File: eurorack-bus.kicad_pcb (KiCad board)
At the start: 2 copper layers, 5 parts, among them J1 Conn_02x08_Odd_Even, J3 Conn_02x08_Odd_Even, J4 Conn_02x08_Odd_Even, J5 Conn_02x08_Odd_Even, J6 Conn_02x08_Odd_Even

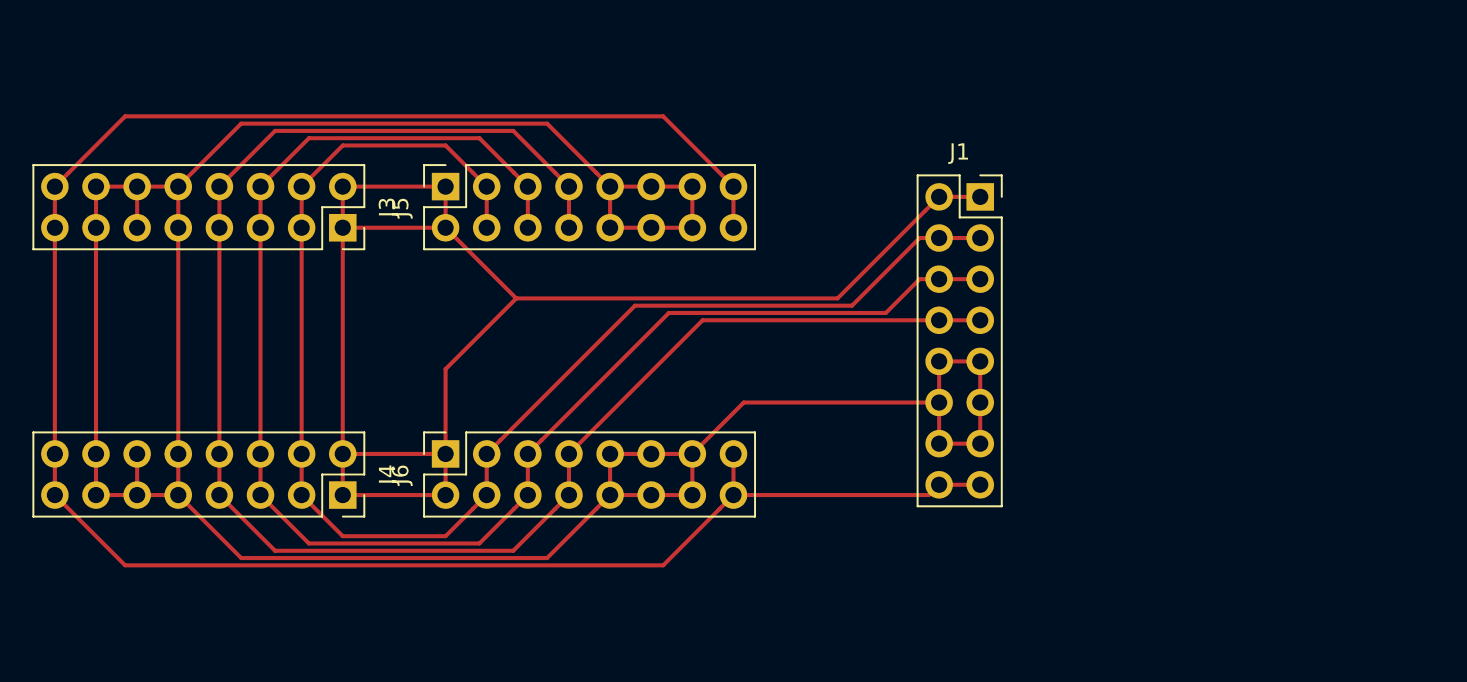
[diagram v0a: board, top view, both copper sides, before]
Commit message: readd conn J2, rm 5v/cv/gt tracks, route
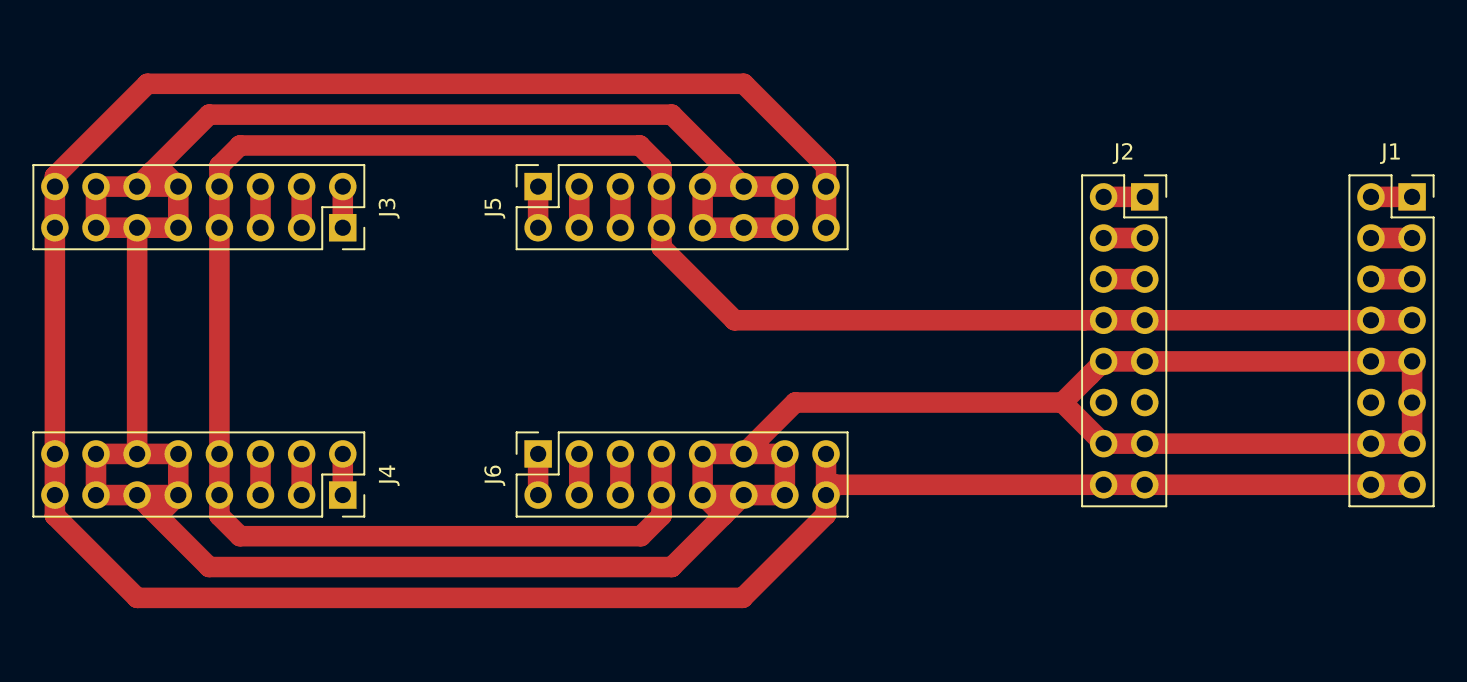
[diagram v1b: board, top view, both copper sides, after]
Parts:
- added J2: Conn_02x08_Odd_Even, Connector_PinSocket_2.54mm:PinSocket_2x08_P2.54mm_Vertical, F.Cu at (151.1, 80.6)
- moved J1 26.7 mm to (167.6, 80.6)
- moved J5 5.72 mm to (113.7, 80.0)
- moved J6 5.72 mm to (113.7, 96.5)
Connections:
- J3 pad 1: Net-(J1-Pad1) -> Net-(J3-Pad1)
- J3 pad 2: Net-(J1-Pad1) -> Net-(J3-Pad1)
- J3 pad 3: Net-(J1-Pad3) -> Net-(J3-Pad3)
- J3 pad 4: Net-(J1-Pad3) -> Net-(J3-Pad3)
- J3 pad 5: Net-(J1-Pad5) -> Net-(J3-Pad5)
- J3 pad 6: Net-(J1-Pad5) -> Net-(J3-Pad5)
- J4 pad 1: Net-(J1-Pad1) -> Net-(J4-Pad1)
- J4 pad 2: Net-(J1-Pad1) -> Net-(J4-Pad1)
- J4 pad 3: Net-(J1-Pad3) -> Net-(J4-Pad3)
- J4 pad 4: Net-(J1-Pad3) -> Net-(J4-Pad3)
- J4 pad 5: Net-(J1-Pad5) -> Net-(J4-Pad5)
- J4 pad 6: Net-(J1-Pad5) -> Net-(J4-Pad5)
- J5 pad 1: Net-(J1-Pad1) -> Net-(J5-Pad1)
- J5 pad 2: Net-(J1-Pad1) -> Net-(J5-Pad1)
- J5 pad 3: Net-(J1-Pad3) -> Net-(J5-Pad3)
- J5 pad 4: Net-(J1-Pad3) -> Net-(J5-Pad3)
- J5 pad 5: Net-(J1-Pad5) -> Net-(J5-Pad5)
- J5 pad 6: Net-(J1-Pad5) -> Net-(J5-Pad5)
- J6 pad 1: Net-(J1-Pad1) -> Net-(J6-Pad1)
- J6 pad 2: Net-(J1-Pad1) -> Net-(J6-Pad1)
- J6 pad 3: Net-(J1-Pad3) -> Net-(J6-Pad3)
- J6 pad 4: Net-(J1-Pad3) -> Net-(J6-Pad3)
- J6 pad 5: Net-(J1-Pad5) -> Net-(J6-Pad5)
- J6 pad 6: Net-(J1-Pad5) -> Net-(J6-Pad5)
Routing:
- net Net-(J1-Pad1): track 98.4 -> 2.54 mm
- net Net-(J1-Pad5): track 94.5 -> 2.54 mm
- net Net-(J1-Pad3): track 87.2 -> 2.54 mm
- net Net-(J1-Pad10): track 175.4 -> 234.7 mm
- net Net-(J1-Pad15): track 130.6 -> 168.9 mm
- net Net-(J1-Pad7): track 101.8 -> 135.3 mm
- net Net-(J6-Pad3): track 0.00 -> 2.59 mm
- net Net-(J6-Pad5): track 0.00 -> 2.54 mm
- net Net-(J6-Pad1): track 0.00 -> 2.54 mm
- net Net-(J4-Pad5): track 0.00 -> 2.54 mm
- net Net-(J4-Pad3): track 0.00 -> 2.54 mm
- net Net-(J4-Pad1): track 0.00 -> 2.54 mm
- net Net-(J5-Pad5): track 0.00 -> 2.54 mm
- net Net-(J5-Pad3): track 0.00 -> 2.54 mm
- net Net-(J5-Pad1): track 0.00 -> 2.54 mm
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- added copper zone on F.Cu, net Net-(J1-Pad10)

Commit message: space things out a little further
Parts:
- moved J5 1.27 mm to (113.7, 78.7)
- moved J6 1.27 mm to (113.7, 97.8)
- moved J3 1.27 mm to (101.6, 81.3)
- moved J4 1.27 mm to (101.6, 100.3)
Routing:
- net Net-(J1-Pad15): track 168.9 -> 172.3 mm
- net Net-(J1-Pad10): track 234.7 -> 237.6 mm
- net Net-(J1-Pad7): track 135.3 -> 137.1 mm

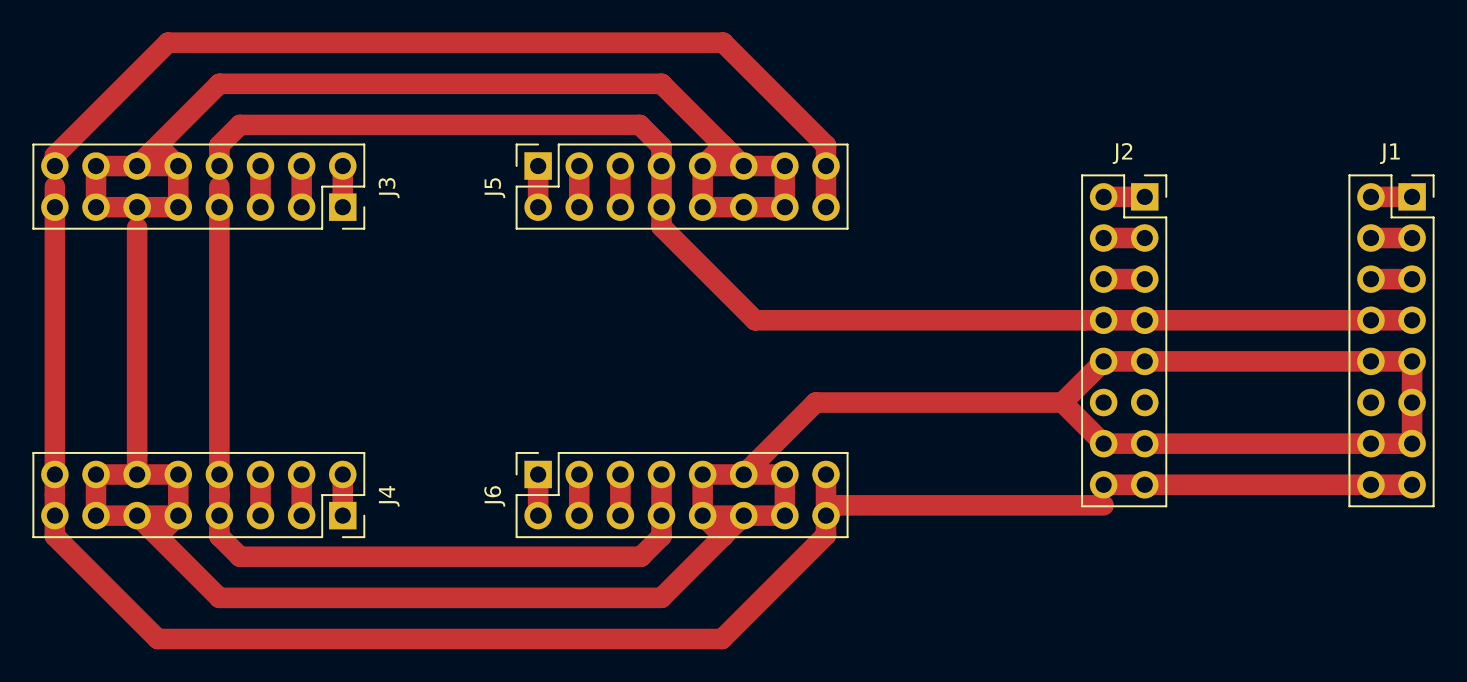
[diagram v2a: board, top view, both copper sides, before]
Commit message: fixup a few traces that should be connected
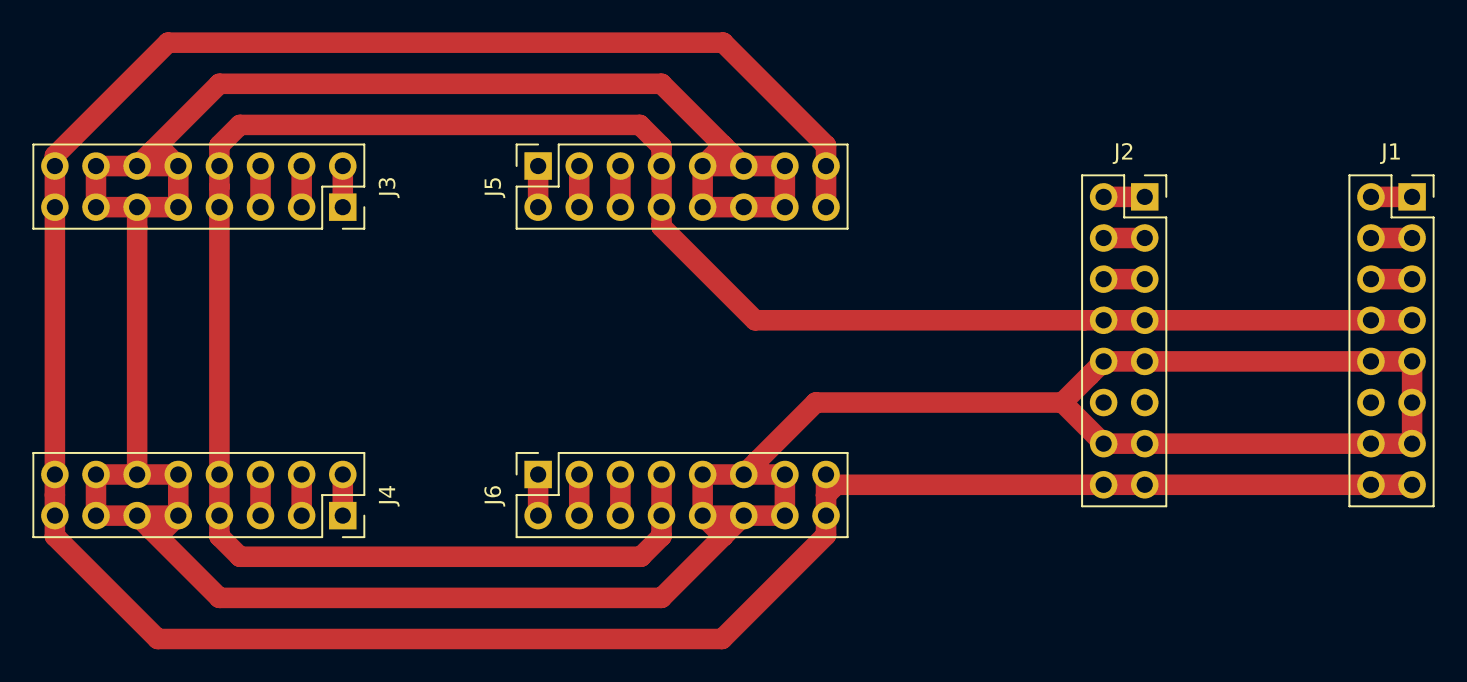
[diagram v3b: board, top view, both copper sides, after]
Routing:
- net Net-(J1-Pad10): track 237.6 -> 238.8 mm
- net Net-(J1-Pad7): track 137.1 -> 138.4 mm
- net Net-(J1-Pad15): track 172.3 -> 173.6 mm
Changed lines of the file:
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@@
     (thickness 1.6)
     (drawings 0)
-    (tracks 103)
+    (tracks 104)
     (zones 0)
     (modules 6)
@@
   (segment (start 93.98 77.47) (end 95.25 76.2) (width 1.27) (layer F.Cu) (net 4))
   (segment (start 95.25 76.2) (end 119.947081 76.2) (width 1.27) (layer F.Cu) (net 4))
-  (segment (start 93.98 99.06) (end 93.98 80.01) (width 1.27) (layer F.Cu) (net 4))
   (segment (start 121.285 78.74) (end 121.285 81.28) (width 1.27) (layer F.Cu) (net 4))
   (segment (start 121.285 97.79) (end 121.285 100.33) (width 1.27) (layer F.Cu) (net 4))
@@
   (segment (start 121.285 101.6) (end 120.015 102.87) (width 1.27) (layer F.Cu) (net 4))
   (segment (start 121.285 100.33) (end 121.285 101.6) (width 1.27) (layer F.Cu) (net 4))
-  (segment (start 93.98 99.06) (end 93.98 100.33) (width 1.27) (layer F.Cu) (net 4))
   (segment (start 147.387919 88.265) (end 148.59 88.265) (width 1.27) (layer F.Cu) (net 4))
   (segment (start 127.067919 88.265) (end 147.387919 88.265) (width 1.27) (layer F.Cu) (net 4))
   (segment (start 121.285 82.482081) (end 127.067919 88.265) (width 1.27) (layer F.Cu) (net 4))
   (segment (start 121.285 81.28) (end 121.285 82.482081) (width 1.27) (layer F.Cu) (net 4))
+  (segment (start 93.98 80.01) (end 93.98 78.74) (width 1.27) (layer F.Cu) (net 4))
+  (segment (start 93.98 100.33) (end 93.98 80.01) (width 1.27) (layer F.Cu) (net 4))
   (segment (start 167.64 90.805) (end 148.59 90.805) (width 1.27) (layer F.Cu) (net 5))
   (segment (start 167.64 95.885) (end 148.59 95.885) (width 1.27) (layer F.Cu) (net 5))
@@
   (segment (start 91.44 97.79) (end 91.44 100.33) (width 1.27) (layer F.Cu) (net 5))
   (segment (start 91.44 100.33) (end 88.9 100.33) (width 1.27) (layer F.Cu) (net 5))
-  (segment (start 88.9 96.52) (end 88.9 82.55) (width 1.27) (layer F.Cu) (net 5))
   (segment (start 88.9 81.28) (end 86.36 81.28) (width 1.27) (layer F.Cu) (net 5))
   (segment (start 86.36 81.28) (end 86.36 78.74) (width 1.27) (layer F.Cu) (net 5))
@@
   (segment (start 123.825 78.74) (end 125.095 77.47) (width 1.27) (layer F.Cu) (net 5))
   (segment (start 126.365 78.74) (end 125.095 77.47) (width 1.27) (layer F.Cu) (net 5))
-  (segment (start 88.9 96.52) (end 88.9 97.79) (width 1.27) (layer F.Cu) (net 5))
   (segment (start 127.214999 96.940001) (end 126.365 97.79) (width 1.27) (layer F.Cu) (net 5))
   (segment (start 130.81 93.345) (end 127.214999 96.940001) (width 1.27) (layer F.Cu) (net 5))
@@
   (segment (start 121.285 73.66) (end 93.98 73.66) (width 1.27) (layer F.Cu) (net 5))
   (segment (start 125.095 77.47) (end 121.285 73.66) (width 1.27) (layer F.Cu) (net 5))
+  (segment (start 88.9 82.55) (end 88.9 81.28) (width 1.27) (layer F.Cu) (net 5))
+  (segment (start 88.9 97.79) (end 88.9 82.55) (width 1.27) (layer F.Cu) (net 5))
   (segment (start 167.64 98.425) (end 148.59 98.425) (width 1.27) (layer F.Cu) (net 6))
-  (segment (start 132.08 99.695) (end 131.445 100.33) (width 1.27) (layer F.Cu) (net 6))
-  (segment (start 148.59 99.695) (end 132.08 99.695) (width 1.27) (layer F.Cu) (net 6))
-  (segment (start 131.445 100.33) (end 131.445 97.79) (width 1.27) (layer F.Cu) (net 6))
-  (segment (start 83.82 99.06) (end 83.82 80.01) (width 1.27) (layer F.Cu) (net 6))
   (segment (start 131.445 78.74) (end 131.445 81.28) (width 1.27) (layer F.Cu) (net 6))
-  (segment (start 83.82 99.06) (end 83.82 100.33) (width 1.27) (layer F.Cu) (net 6))
   (segment (start 83.82 101.6) (end 83.82 100.33) (width 1.27) (layer F.Cu) (net 6))
   (segment (start 125.027081 107.95) (end 90.17 107.95) (width 1.27) (layer F.Cu) (net 6))
@@
   (segment (start 131.445 77.47) (end 125.095 71.12) (width 1.27) (layer F.Cu) (net 6))
   (segment (start 131.445 78.74) (end 131.445 77.47) (width 1.27) (layer F.Cu) (net 6))
+  (segment (start 132.08 98.425) (end 131.445 99.06) (width 1.27) (layer F.Cu) (net 6))
+  (segment (start 131.445 99.06) (end 131.445 97.79) (width 1.27) (layer F.Cu) (net 6))
+  (segment (start 148.59 98.425) (end 132.08 98.425) (width 1.27) (layer F.Cu) (net 6))
+  (segment (start 131.445 100.33) (end 131.445 99.06) (width 1.27) (layer F.Cu) (net 6))
+  (segment (start 83.82 99.06) (end 83.82 100.33) (width 1.27) (layer F.Cu) (net 6))
+  (segment (start 83.82 78.74) (end 83.82 99.06) (width 1.27) (layer F.Cu) (net 6))
   (segment (start 148.59 80.645) (end 151.13 80.645) (width 1.27) (layer F.Cu) (net 7))
   (segment (start 148.59 83.185) (end 151.13 83.185) (width 1.27) (layer F.Cu) (net 8))

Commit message: add traces for 5v line throughout
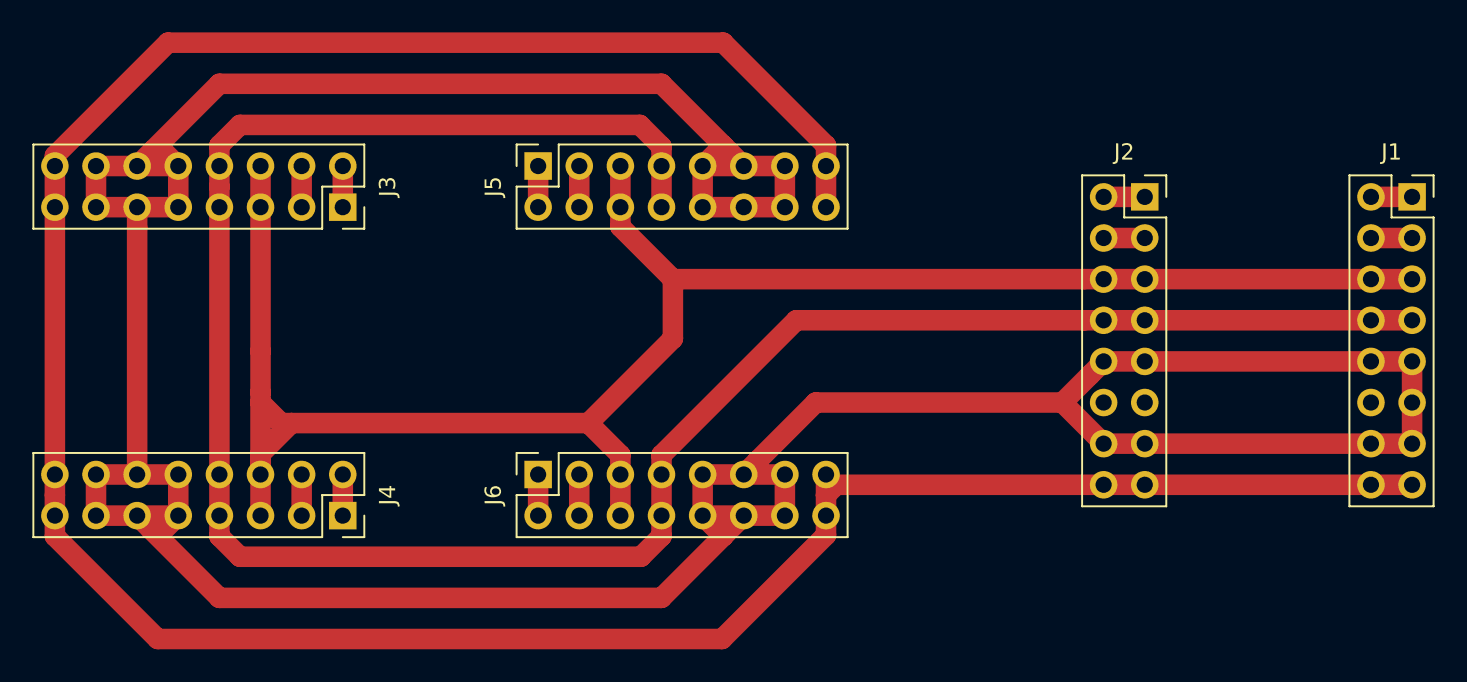
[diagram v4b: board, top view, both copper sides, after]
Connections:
- J2 pad 5: Net-(J2-Pad5) -> Net-(J1-Pad5)
- J2 pad 6: Net-(J2-Pad5) -> Net-(J1-Pad5)
- J3 pad 5: Net-(J3-Pad5) -> Net-(J1-Pad5)
- J3 pad 6: Net-(J3-Pad5) -> Net-(J1-Pad5)
- J4 pad 5: Net-(J4-Pad5) -> Net-(J1-Pad5)
- J4 pad 6: Net-(J4-Pad5) -> Net-(J1-Pad5)
- J5 pad 5: Net-(J5-Pad5) -> Net-(J1-Pad5)
- J5 pad 6: Net-(J5-Pad5) -> Net-(J1-Pad5)
- J6 pad 5: Net-(J6-Pad5) -> Net-(J1-Pad5)
- J6 pad 6: Net-(J6-Pad5) -> Net-(J1-Pad5)
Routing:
- net Net-(J1-Pad5): track 2.54 -> 117.9 mm
- net Net-(J5-Pad5): track 2.54 -> 0.00 mm
- net Net-(J3-Pad5): track 2.54 -> 0.00 mm
- net Net-(J6-Pad5): track 2.54 -> 0.00 mm
- net Net-(J4-Pad5): track 2.54 -> 0.00 mm
- net Net-(J2-Pad5): track 2.54 -> 0.00 mm
- net Net-(J1-Pad7): track 138.4 -> 139.4 mm
